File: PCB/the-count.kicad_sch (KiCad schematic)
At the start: 24 parts

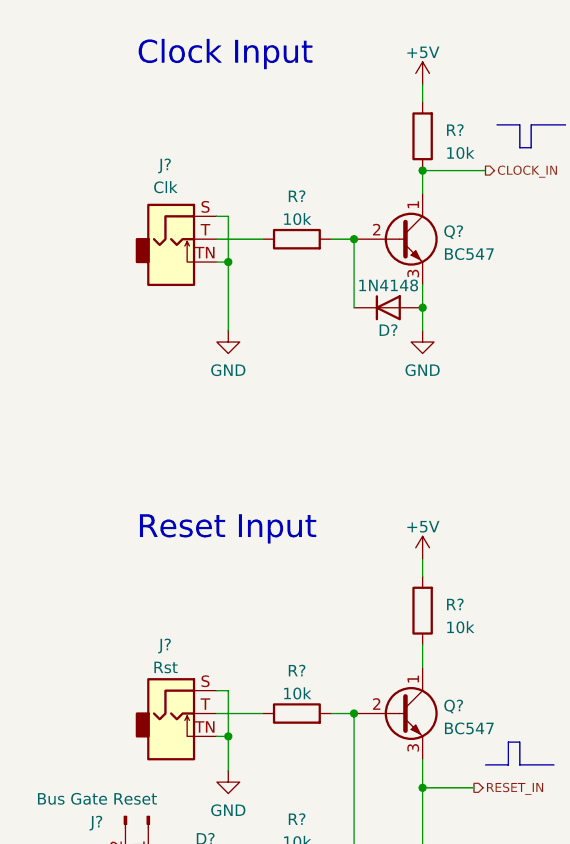
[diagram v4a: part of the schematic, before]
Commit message: :wrench: Set CLIFF footprints for the jacks
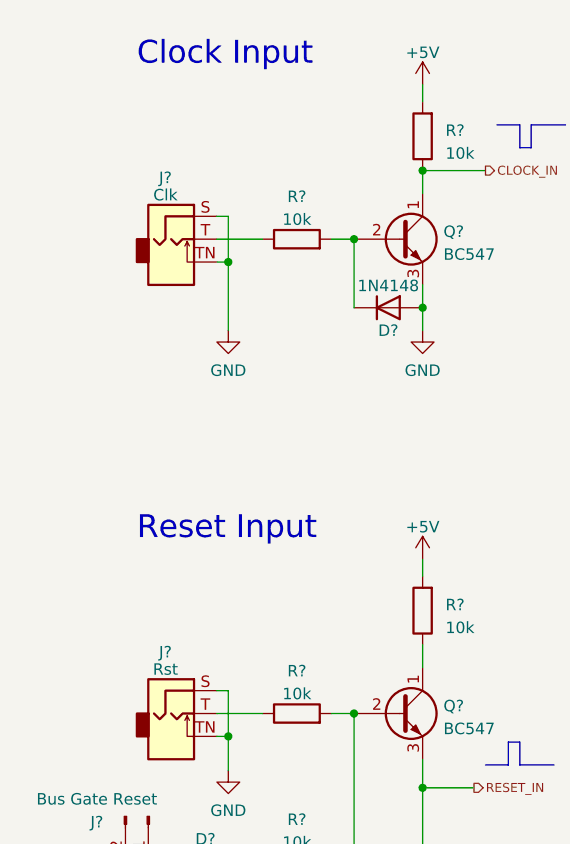
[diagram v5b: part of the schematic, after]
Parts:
- J? (x2): footprint moPsy:Jack_3.5mm_QingPu_WQP-PJ398SM_Vertical_CircularHoles_Centered -> moPsy:CLIFF 3.5mm S6 Mono Jack Socket
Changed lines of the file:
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@@
   (symbol (lib_id "Connector:AudioJack2_Ground_SwitchT") (at 31.115 46.355 0) (unit 1)
     (in_bom yes) (on_board yes) (dnp no) (fields_autoplaced)
-    (property "Reference" "J?" (at 30.48 38.1 0)
+    (property "Reference" "J?" (at 30.48 39.5351 0)
       (effects (font (size 1.27 1.27)))
     )
-    (property "Value" "Clk" (at 30.48 40.64 0)
+    (property "Value" "Clk" (at 30.48 41.4561 0)
       (effects (font (size 1.27 1.27)))
     )
-    (property "Footprint" "moPsy:Jack_3.5mm_QingPu_WQP-PJ398SM_Vertical_CircularHoles_Centered" (at 31.115 46.355 0)
+    (property "Footprint" "moPsy:CLIFF 3.5mm S6 Mono Jack Socket" (at 31.115 46.355 0)
       (effects (font (size 1.27 1.27)) hide)
     )
@@
   (symbol (lib_id "Connector:AudioJack2_Ground_SwitchT") (at 31.115 99.06 0) (unit 1)
     (in_bom yes) (on_board yes) (dnp no) (fields_autoplaced)
-    (property "Reference" "J?" (at 30.48 91.44 0)
+    (property "Reference" "J?" (at 30.48 92.2401 0)
       (effects (font (size 1.27 1.27)))
     )
-    (property "Value" "Rst" (at 30.48 93.98 0)
+    (property "Value" "Rst" (at 30.48 94.1611 0)
       (effects (font (size 1.27 1.27)))
     )
-    (property "Footprint" "moPsy:Jack_3.5mm_QingPu_WQP-PJ398SM_Vertical_CircularHoles_Centered" (at 31.115 99.06 0)
+    (property "Footprint" "moPsy:CLIFF 3.5mm S6 Mono Jack Socket" (at 31.115 99.06 0)
       (effects (font (size 1.27 1.27)) hide)
     )
